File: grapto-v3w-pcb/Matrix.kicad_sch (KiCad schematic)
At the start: 2 parts

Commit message: Think i got modules working.
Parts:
- added D?: D, symbol Device:D
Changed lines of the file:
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@@
 (kicad_sch (version 20211123) (generator eeschema)
   (paper "A4")
-  (symbol (lib_id "Device:D") (at 69.215 37.465 180) (unit 1)
+  (symbol (lib_id "Device:D") (at 69.215 37.465 180)
     (in_bom yes) (on_board yes) (fields_autoplaced)
     (property "Reference" "D?" (id 0) (at 69.215 32.4952 0))
@@
     (pin "2")
   )
-  (symbol (lib_id "Switch:SW_Push") (at 54.61 37.465 0) (unit 1)
+  (symbol (lib_id "Switch:SW_Push") (at 54.61 37.465 0)
     (in_bom yes) (on_board yes) (fields_autoplaced)
     (property "Reference" "SW?" (id 0) (at 54.61 30.8442 0))
@@
       (effects (font (size 1.27 1.27)) hide)
     )
+    (pin "1")
+    (pin "2")
+  )
+  (symbol (lib_id "Device:D") (at 95.885 41.91 0)
+    (in_bom yes) (on_board yes) (fields_autoplaced)
+    (property "Reference" "D?" (id 0) (at 95.885 36.9402 0))
+    (property "Value" "D" (id 1) (at 95.885 39.4771 0))
+    (property "Footprint" "" (id 2) (at 95.885 41.91 0)
+      (effects (font (size 1.27 1.27)) hide)
+    )
+    (property "Datasheet" "~" (id 3) (at 95.885 41.91 0)
+      (effects (font (size 1.27 1.27)) hide)
+    )

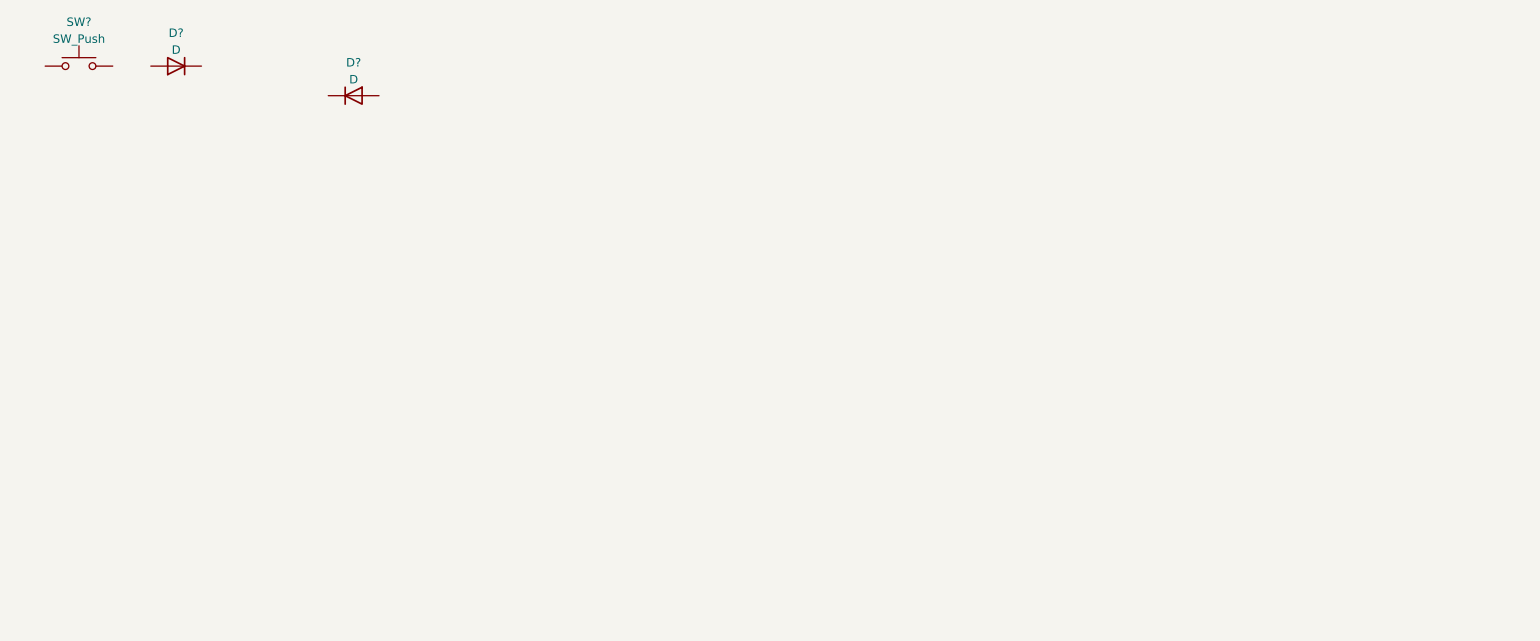
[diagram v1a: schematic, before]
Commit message: Added keymatrix.
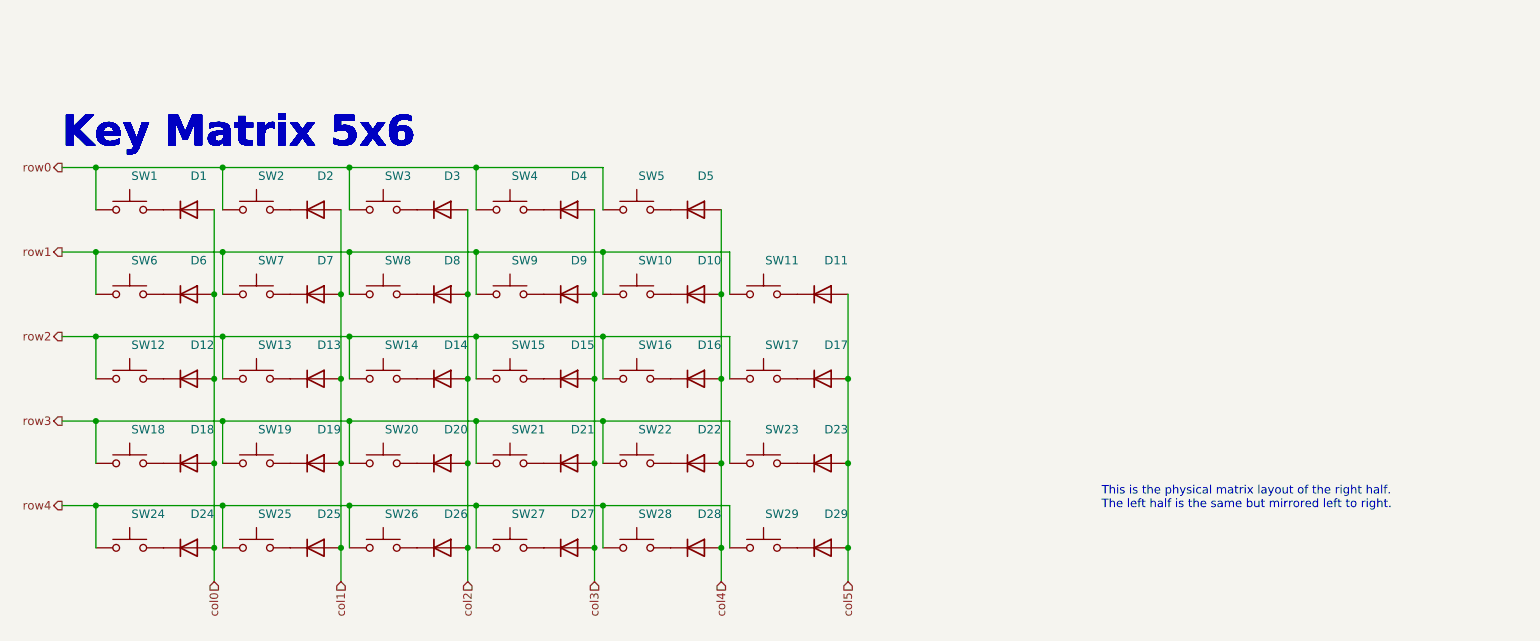
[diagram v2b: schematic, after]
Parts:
- removed D? (x2): D, symbol Device:D
- removed SW?: SW_Push, symbol Switch:SW_Push
- added D1, D10, D11, D12, D13, D14, D15, D16, D17, D18, D19, D2, D20, D21, D22, D23, D24, D25, D26, D27, D28, D29, D3, D4, D5, D6, D7, D8, D9: ~, symbol Device:D
- added SW1, SW10, SW11, SW12, SW13, SW14, SW15, SW16, SW17, SW18, SW19, SW2, SW20, SW21, SW22, SW23, SW24, SW25, SW26, SW27, SW28, SW29, SW3, SW4, SW5, SW6, SW7, SW8, SW9: ~, symbol Switch:SW_Push
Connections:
- new net: D16.1 (K), SW16.2
- new net: D10.1 (K), SW10.2
- new net: D15.1 (K), SW15.2
- new net: D22.1 (K), SW22.2
- new net: D17.1 (K), SW17.2
- new net: D19.1 (K), SW19.2
- new net: D5.1 (K), SW5.2
- new net: D14.1 (K), SW14.2
- new net: D27.1 (K), SW27.2
- new net: D9.1 (K), SW9.2
- new net: D20.1 (K), SW20.2
- new net: D13.1 (K), SW13.2
- new net: D18.1 (K), SW18.2
- new net: D6.1 (K), SW6.2
- new net: D11.1 (K), SW11.2
- new net: D4.1 (K), SW4.2
- new net: D29.1 (K), SW29.2
- new net: D23.1 (K), SW23.2
- new net: D12.1 (K), SW12.2
- new net: D3.1 (K), SW3.2
- new net: D2.1 (K), SW2.2
- new net: D7.1 (K), SW7.2
- new net: D8.1 (K), SW8.2
- new net: D26.1 (K), SW26.2
- new net: D24.1 (K), SW24.2
- new net: D25.1 (K), SW25.2
- new net: D28.1 (K), SW28.2
- new net: D1.1 (K), SW1.2
- new net: D21.1 (K), SW21.2
- new net col0: D1.2 (A), D12.2 (A), D18.2 (A), D24.2 (A), D6.2 (A)
- new net col1: D13.2 (A), D19.2 (A), D2.2 (A), D25.2 (A), D7.2 (A)
- new net col2: D14.2 (A), D20.2 (A), D26.2 (A), D3.2 (A), D8.2 (A)
- new net col3: D15.2 (A), D21.2 (A), D27.2 (A), D4.2 (A), D9.2 (A)
- new net col4: D10.2 (A), D16.2 (A), D22.2 (A), D28.2 (A), D5.2 (A)
- new net col5: D11.2 (A), D17.2 (A), D23.2 (A), D29.2 (A)
- new net row0: SW1.1, SW2.1, SW3.1, SW4.1, SW5.1
- new net row1: SW10.1, SW11.1, SW6.1, SW7.1, SW8.1, SW9.1
- new net row2: SW12.1, SW13.1, SW14.1, SW15.1, SW16.1, SW17.1
- new net row3: SW18.1, SW19.1, SW20.1, SW21.1, SW22.1, SW23.1
- new net row4: SW24.1, SW25.1, SW26.1, SW27.1, SW28.1, SW29.1
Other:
- note added: "Key Matrix 5x6"
- note added: "This is the physical matrix layout of the right half. The left half is the same but mirrored left to right."

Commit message: Footprints done.
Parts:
- SW31: renamed from SW2; footprint (none) -> choc:SW_PG1350
- SW32: renamed from SW3; footprint (none) -> choc:SW_PG1350
- SW33: renamed from SW4; footprint (none) -> choc:SW_PG1350
- SW34: renamed from SW5; footprint (none) -> choc:SW_PG1350
- SW35: renamed from SW6; footprint (none) -> choc:SW_PG1350
- SW36: renamed from SW7; footprint (none) -> choc:SW_PG1350
- SW37: renamed from SW8; footprint (none) -> choc:SW_PG1350
- SW38: renamed from SW9; footprint (none) -> choc:SW_PG1350
- SW39: renamed from SW10; footprint (none) -> choc:SW_PG1350
- SW40: renamed from SW11; footprint (none) -> choc:SW_PG1350
- SW41: renamed from SW12; footprint (none) -> choc:SW_PG1350
- SW42: renamed from SW13; footprint (none) -> choc:SW_PG1350
- SW43: renamed from SW14; footprint (none) -> choc:SW_PG1350
- SW44: renamed from SW15; footprint (none) -> choc:SW_PG1350
- SW45: renamed from SW16; footprint (none) -> choc:SW_PG1350
- SW46: renamed from SW17; footprint (none) -> choc:SW_PG1350
- SW47: renamed from SW18; footprint (none) -> choc:SW_PG1350
- SW48: renamed from SW19; footprint (none) -> choc:SW_PG1350
- SW49: renamed from SW20; footprint (none) -> choc:SW_PG1350
- SW50: renamed from SW21; footprint (none) -> choc:SW_PG1350
- SW51: renamed from SW22; footprint (none) -> choc:SW_PG1350
- SW52: renamed from SW23; footprint (none) -> choc:SW_PG1350
- SW53: renamed from SW24; footprint (none) -> choc:SW_PG1350
- SW54: renamed from SW25; footprint (none) -> choc:SW_PG1350
- SW55: renamed from SW26; footprint (none) -> choc:SW_PG1350
- SW56: renamed from SW27; footprint (none) -> choc:SW_PG1350
- SW57: renamed from SW28; footprint (none) -> choc:SW_PG1350
- SW58: renamed from SW29; footprint (none) -> choc:SW_PG1350
- renumbered D1 to D32, D2 to D33, D3 to D34, D4 to D35, D5 to D36, D6 to D37, D7 to D38, D8 to D39, D9 to D40, D10 to D41, D11 to D42, D12 to D43, D13 to D44, D14 to D45, D15 to D46, D16 to D47, D17 to D48, D18 to D49, D19 to D50, D20 to D51, D21 to D52, D22 to D53, D23 to D54, D24 to D55, D25 to D56, D26 to D57, D27 to D58, D28 to D59, D29 to D60, SW1 to SW30

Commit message: Fixed 3d model paths for pcb.
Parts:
- D32, D33, D34, D35, D36, D37, D38, D39, D40, D41, D42, D43, D44, D45, D46, D47, D48, D49, D50, D51, D52, D53, D54, D55, D56, D57, D58, D59, D60: footprint (none) -> Diode_SMD:D_SOD-123
- SW31, SW32, SW33, SW34, SW35, SW36, SW37, SW38, SW39, SW40, SW41, SW42, SW43, SW44, SW45, SW46, SW47, SW48, SW49, SW50, SW51, SW52, SW53, SW54, SW55, SW56, SW57, SW58: footprint choc:SW_PG1350 -> (none)

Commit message: Began case rework.
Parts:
- SW30, SW31, SW32, SW33, SW34, SW35, SW36, SW37, SW38, SW39, SW40, SW41, SW42, SW43, SW44, SW45, SW46, SW47, SW48, SW49, SW50, SW51, SW52, SW53, SW54, SW55, SW56, SW57, SW58: footprint (none) -> Switch_Keyboard_Kailh:SW_Kailh_Choc_V1_1.00u
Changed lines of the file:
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@@
     )
     (property "Value" "~" (id 1) (at 119.38 86.995 0))
-    (property "Footprint" "" (id 2) (at 119.38 79.375 0)
+    (property "Footprint" "Switch_Keyboard_Kailh:SW_Kailh_Choc_V1_1.00u" (id 2) (at 119.38 79.375 0)
       (effects (font (size 1.27 1.27)) hide)
     )
@@
     )
     (property "Value" "~" (id 1) (at 138.43 99.695 0))
-    (property "Footprint" "" (id 2) (at 138.43 92.075 0)
+    (property "Footprint" "Switch_Keyboard_Kailh:SW_Kailh_Choc_V1_1.00u" (id 2) (at 138.43 92.075 0)
       (effects (font (size 1.27 1.27)) hide)
     )
@@
     )
     (property "Value" "~" (id 1) (at 81.28 99.695 0))
-    (property "Footprint" "" (id 2) (at 81.28 92.075 0)
+    (property "Footprint" "Switch_Keyboard_Kailh:SW_Kailh_Choc_V1_1.00u" (id 2) (at 81.28 92.075 0)
       (effects (font (size 1.27 1.27)) hide)
     )
@@
     )
     (property "Value" "~" (id 1) (at 138.43 61.595 0))
-    (property "Footprint" "" (id 2) (at 138.43 53.975 0)
+    (property "Footprint" "Switch_Keyboard_Kailh:SW_Kailh_Choc_V1_1.00u" (id 2) (at 138.43 53.975 0)
       (effects (font (size 1.27 1.27)) hide)
     )
@@
     )
     (property "Value" "~" (id 1) (at 100.33 86.995 0))
-    (property "Footprint" "" (id 2) (at 100.33 79.375 0)
+    (property "Footprint" "Switch_Keyboard_Kailh:SW_Kailh_Choc_V1_1.00u" (id 2) (at 100.33 79.375 0)
       (effects (font (size 1.27 1.27)) hide)
     )
@@
     )
     (property "Value" "~" (id 1) (at 119.38 74.295 0))
-    (property "Footprint" "" (id 2) (at 119.38 66.675 0)
+    (property "Footprint" "Switch_Keyboard_Kailh:SW_Kailh_Choc_V1_1.00u" (id 2) (at 119.38 66.675 0)
       (effects (font (size 1.27 1.27)) hide)
     )
@@
     )
     (property "Value" "~" (id 1) (at 157.48 74.295 0))
-    (property "Footprint" "" (id 2) (at 157.48 66.675 0)
+    (property "Footprint" "Switch_Keyboard_Kailh:SW_Kailh_Choc_V1_1.00u" (id 2) (at 157.48 66.675 0)
       (effects (font (size 1.27 1.27)) hide)
     )
@@
     )
     (property "Value" "~" (id 1) (at 157.48 112.395 0))
-    (property "Footprint" "" (id 2) (at 157.48 104.775 0)
+    (property "Footprint" "Switch_Keyboard_Kailh:SW_Kailh_Choc_V1_1.00u" (id 2) (at 157.48 104.775 0)
       (effects (font (size 1.27 1.27)) hide)
     )
@@
     )
     (property "Value" "~" (id 1) (at 138.43 74.295 0))
-    (property "Footprint" "" (id 2) (at 138.43 66.675 0)
+    (property "Footprint" "Switch_Keyboard_Kailh:SW_Kailh_Choc_V1_1.00u" (id 2) (at 138.43 66.675 0)
       (effects (font (size 1.27 1.27)) hide)
     )
@@
     )
     (property "Value" "~" (id 1) (at 62.23 86.995 0))
-    (property "Footprint" "" (id 2) (at 62.23 79.375 0)
+    (property "Footprint" "Switch_Keyboard_Kailh:SW_Kailh_Choc_V1_1.00u" (id 2) (at 62.23 79.375 0)
       (effects (font (size 1.27 1.27)) hide)
     )
@@
     )
     (property "Value" "~" (id 1) (at 81.28 74.295 0))
-    (property "Footprint" "" (id 2) (at 81.28 66.675 0)
+    (property "Footprint" "Switch_Keyboard_Kailh:SW_Kailh_Choc_V1_1.00u" (id 2) (at 81.28 66.675 0)
       (effects (font (size 1.27 1.27)) hide)
     )
@@
     )
     (property "Value" "~" (id 1) (at 100.33 74.295 0))
-    (property "Footprint" "" (id 2) (at 100.33 66.675 0)
+    (property "Footprint" "Switch_Keyboard_Kailh:SW_Kailh_Choc_V1_1.00u" (id 2) (at 100.33 66.675 0)
       (effects (font (size 1.27 1.27)) hide)
     )
@@
     )
     (property "Value" "~" (id 1) (at 62.23 74.295 0))
-    (property "Footprint" "" (id 2) (at 62.23 66.675 0)
+    (property "Footprint" "Switch_Keyboard_Kailh:SW_Kailh_Choc_V1_1.00u" (id 2) (at 62.23 66.675 0)
       (effects (font (size 1.27 1.27)) hide)
     )
@@
     )
     (property "Value" "~" (id 1) (at 100.33 61.595 0))
-    (property "Footprint" "" (id 2) (at 100.33 53.975 0)
+    (property "Footprint" "Switch_Keyboard_Kailh:SW_Kailh_Choc_V1_1.00u" (id 2) (at 100.33 53.975 0)
       (effects (font (size 1.27 1.27)) hide)
     )
@@
     )
     (property "Value" "~" (id 1) (at 119.38 61.595 0))
-    (property "Footprint" "" (id 2) (at 119.38 53.975 0)
+    (property "Footprint" "Switch_Keyboard_Kailh:SW_Kailh_Choc_V1_1.00u" (id 2) (at 119.38 53.975 0)
       (effects (font (size 1.27 1.27)) hide)
     )
@@
     )
     (property "Value" "~" (id 1) (at 62.23 112.395 0))
-    (property "Footprint" "" (id 2) (at 62.23 104.775 0)
+    (property "Footprint" "Switch_Keyboard_Kailh:SW_Kailh_Choc_V1_1.00u" (id 2) (at 62.23 104.775 0)
       (effects (font (size 1.27 1.27)) hide)
     )
@@
     )
     (property "Value" "~" (id 1) (at 81.28 112.395 0))
-    (property "Footprint" "" (id 2) (at 81.28 104.775 0)
+    (property "Footprint" "Switch_Keyboard_Kailh:SW_Kailh_Choc_V1_1.00u" (id 2) (at 81.28 104.775 0)
       (effects (font (size 1.27 1.27)) hide)
     )
@@
     )
     (property "Value" "~" (id 1) (at 81.28 86.995 0))
-    (property "Footprint" "" (id 2) (at 81.28 79.375 0)
+    (property "Footprint" "Switch_Keyboard_Kailh:SW_Kailh_Choc_V1_1.00u" (id 2) (at 81.28 79.375 0)
       (effects (font (size 1.27 1.27)) hide)
     )
@@
     )
     (property "Value" "~" (id 1) (at 138.43 112.395 0))
-    (property "Footprint" "" (id 2) (at 138.43 104.775 0)
+    (property "Footprint" "Switch_Keyboard_Kailh:SW_Kailh_Choc_V1_1.00u" (id 2) (at 138.43 104.775 0)
       (effects (font (size 1.27 1.27)) hide)
     )
@@
     )
     (property "Value" "~" (id 1) (at 157.48 99.695 0))
-    (property "Footprint" "" (id 2) (at 157.48 92.075 0)
+    (property "Footprint" "Switch_Keyboard_Kailh:SW_Kailh_Choc_V1_1.00u" (id 2) (at 157.48 92.075 0)
       (effects (font (size 1.27 1.27)) hide)
     )
@@
     )
     (property "Value" "~" (id 1) (at 138.43 86.995 0))
-    (property "Footprint" "" (id 2) (at 138.43 79.375 0)
+    (property "Footprint" "Switch_Keyboard_Kailh:SW_Kailh_Choc_V1_1.00u" (id 2) (at 138.43 79.375 0)
       (effects (font (size 1.27 1.27)) hide)
     )
@@
     )
     (property "Value" "~" (id 1) (at 119.38 99.695 0))
-    (property "Footprint" "" (id 2) (at 119.38 92.075 0)
+    (property "Footprint" "Switch_Keyboard_Kailh:SW_Kailh_Choc_V1_1.00u" (id 2) (at 119.38 92.075 0)
       (effects (font (size 1.27 1.27)) hide)
     )
@@
     )
     (property "Value" "~" (id 1) (at 157.48 86.995 0))
-    (property "Footprint" "" (id 2) (at 157.48 79.375 0)
+    (property "Footprint" "Switch_Keyboard_Kailh:SW_Kailh_Choc_V1_1.00u" (id 2) (at 157.48 79.375 0)
       (effects (font (size 1.27 1.27)) hide)
     )
@@
     )
     (property "Value" "~" (id 1) (at 100.33 112.395 0))
-    (property "Footprint" "" (id 2) (at 100.33 104.775 0)
+    (property "Footprint" "Switch_Keyboard_Kailh:SW_Kailh_Choc_V1_1.00u" (id 2) (at 100.33 104.775 0)
       (effects (font (size 1.27 1.27)) hide)
     )
@@
     )
     (property "Value" "~" (id 1) (at 62.23 99.695 0))
-    (property "Footprint" "" (id 2) (at 62.23 92.075 0)
+    (property "Footprint" "Switch_Keyboard_Kailh:SW_Kailh_Choc_V1_1.00u" (id 2) (at 62.23 92.075 0)
       (effects (font (size 1.27 1.27)) hide)
     )
@@
     )
     (property "Value" "~" (id 1) (at 62.23 61.595 0))
-    (property "Footprint" "" (id 2) (at 62.23 53.975 0)
+    (property "Footprint" "Switch_Keyboard_Kailh:SW_Kailh_Choc_V1_1.00u" (id 2) (at 62.23 53.975 0)
       (effects (font (size 1.27 1.27)) hide)
     )
@@
     )
     (property "Value" "~" (id 1) (at 119.38 112.395 0))
-    (property "Footprint" "" (id 2) (at 119.38 104.775 0)
+    (property "Footprint" "Switch_Keyboard_Kailh:SW_Kailh_Choc_V1_1.00u" (id 2) (at 119.38 104.775 0)
       (effects (font (size 1.27 1.27)) hide)
     )
@@
     )
     (property "Value" "~" (id 1) (at 100.33 99.695 0))
-    (property "Footprint" "" (id 2) (at 100.33 92.075 0)
+    (property "Footprint" "Switch_Keyboard_Kailh:SW_Kailh_Choc_V1_1.00u" (id 2) (at 100.33 92.075 0)
       (effects (font (size 1.27 1.27)) hide)
     )
@@
     )
     (property "Value" "~" (id 1) (at 81.28 61.595 0))
-    (property "Footprint" "" (id 2) (at 81.28 53.975 0)
-      (effects (font (size 1.27 1.27)) hide)
-    )
+    (property "Footprint" "Switch_Keyboard_Kailh:SW_Kailh_Choc_V1_1.00u" (id 2) (at 81.28 53.975 0)
+      (effects (font (size 1.27 1.27)) hide)
+    )
